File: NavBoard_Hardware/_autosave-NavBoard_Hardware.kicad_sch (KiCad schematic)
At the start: 0 parts

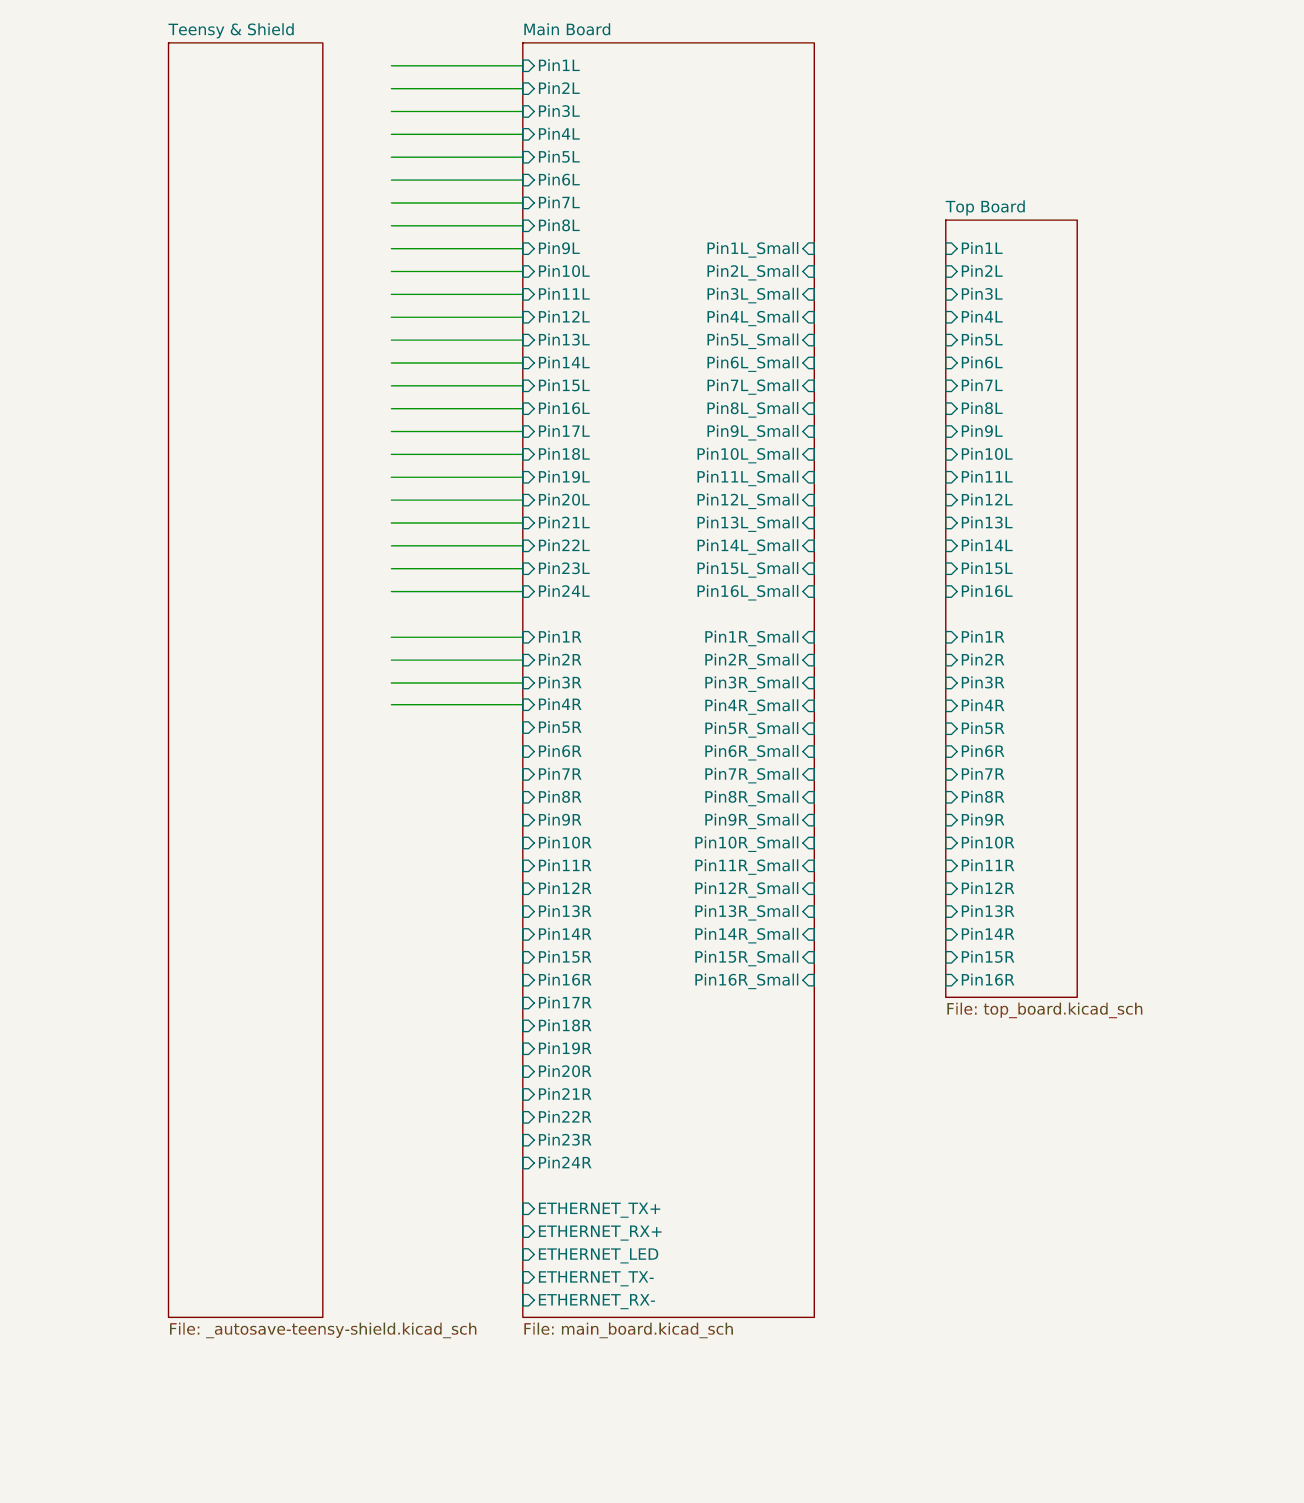
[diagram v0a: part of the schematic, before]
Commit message: Added connectors, cleaned up file directory
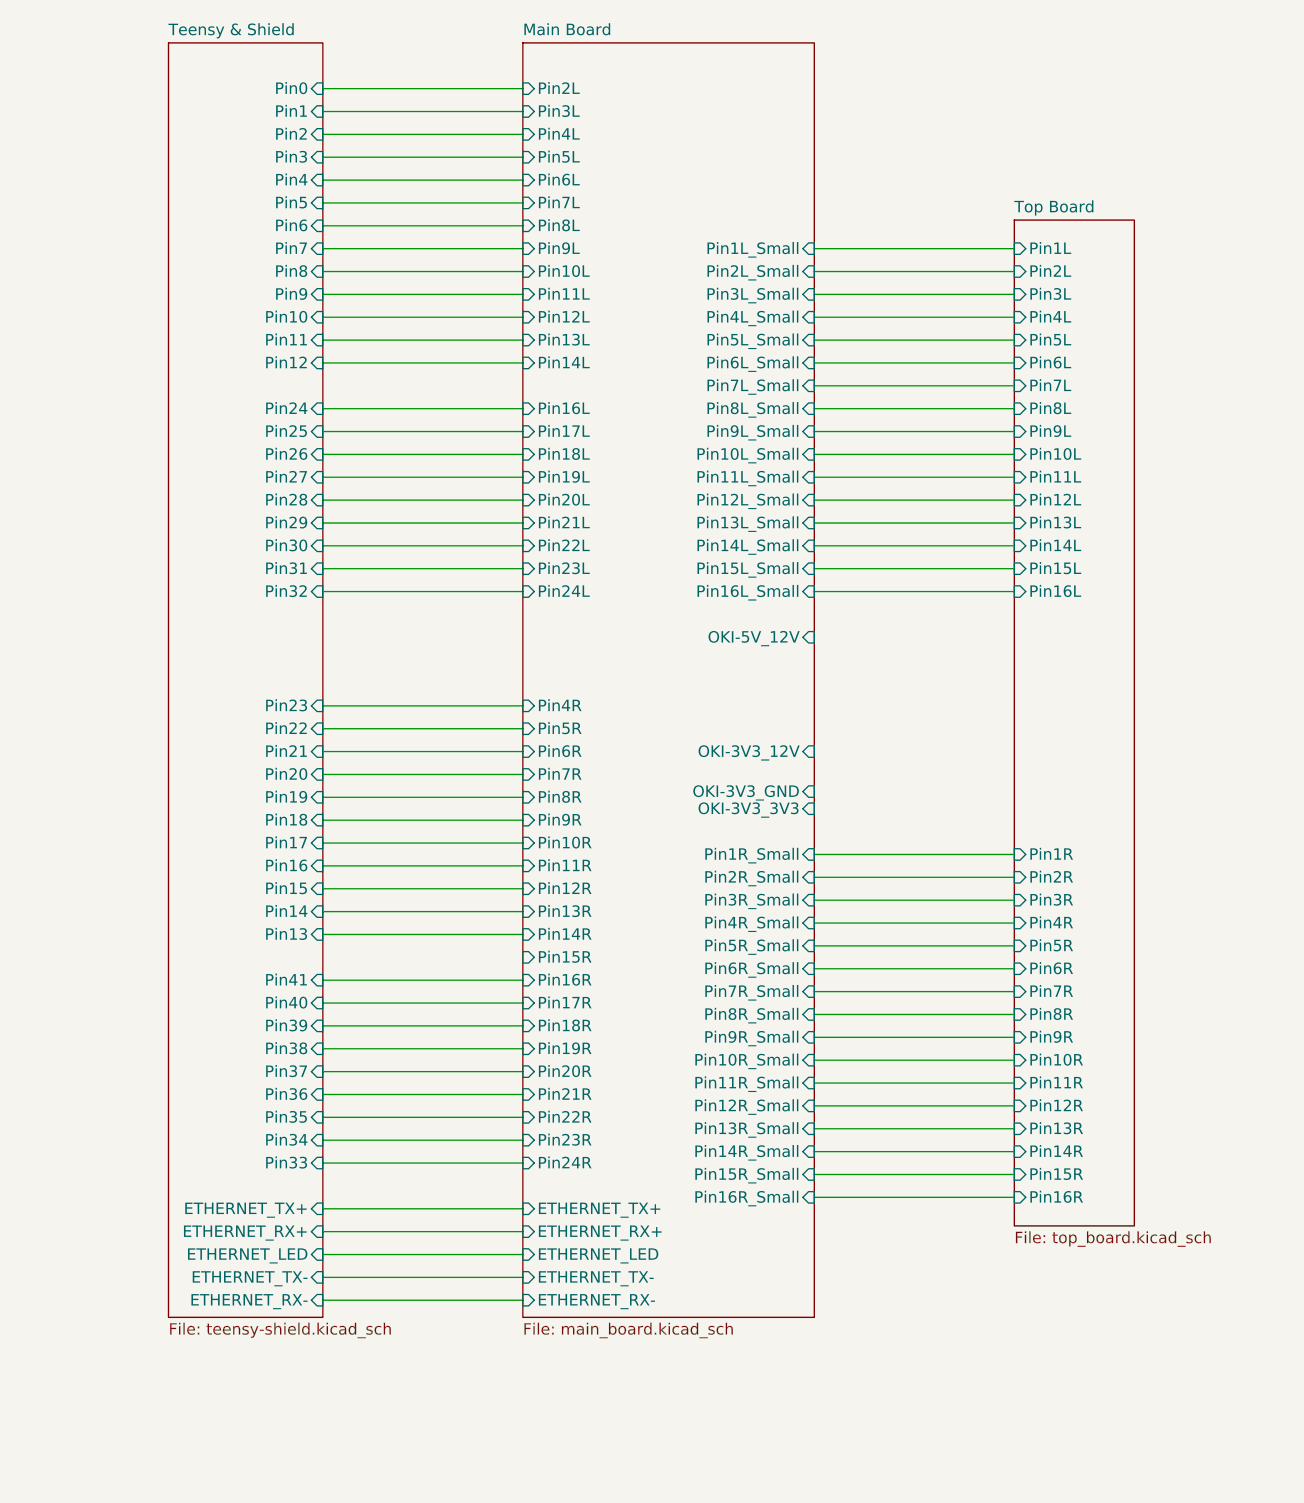
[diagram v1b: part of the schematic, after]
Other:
- sheet Main Board ports: added OKI-3V3_12V, OKI-3V3_3V3, OKI-3V3_GND, OKI-5V_12V; removed Pin15L, Pin1L, Pin1R, Pin2R, Pin3R
- sheet Teensy & Shield: file _autosave-teensy-shield.kicad_sch -> teensy-shield.kicad_sch
- sheet Teensy & Shield ports: added ETHERNET_LED, ETHERNET_RX+, ETHERNET_RX-, ETHERNET_TX+, ETHERNET_TX-, Pin0, Pin1, Pin10, Pin11, Pin12, Pin13, Pin14, Pin15, Pin16, Pin17, Pin18, Pin19, Pin2, Pin20, Pin21, Pin22, Pin23, Pin24, Pin25, Pin26, Pin27, Pin28, Pin29, Pin3, Pin30, Pin31, Pin32, Pin33, Pin34, Pin35, Pin36, Pin37, Pin38, Pin39, Pin4, Pin40, Pin41, Pin5, Pin6, Pin7, Pin8, Pin9; removed none
